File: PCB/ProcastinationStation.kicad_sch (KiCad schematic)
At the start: 19 parts, among them J1 Conn_01x14_Socket, SW1 Up, SW10 X, SW11 L1, SW12 R2, SW13 Right, SW14 Y, SW2 A, SW3 Start, SW4 R1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

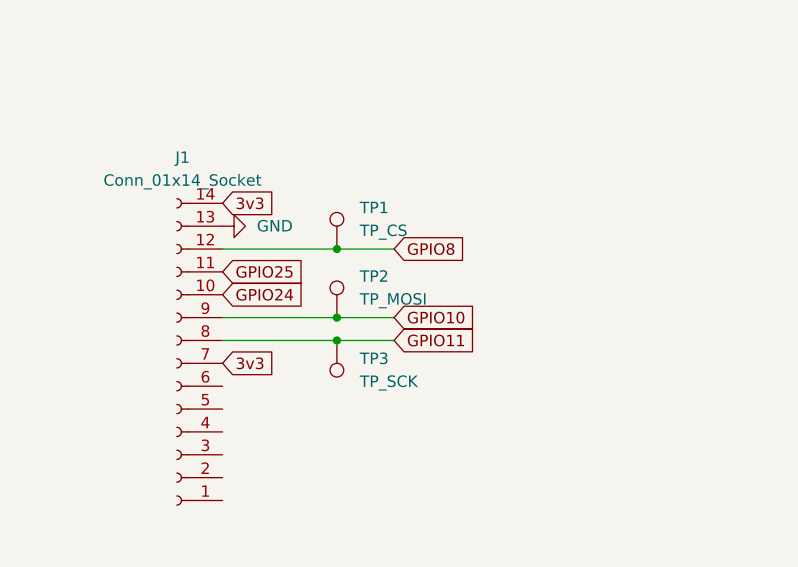
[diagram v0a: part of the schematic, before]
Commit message: Update PCB schematic and layout
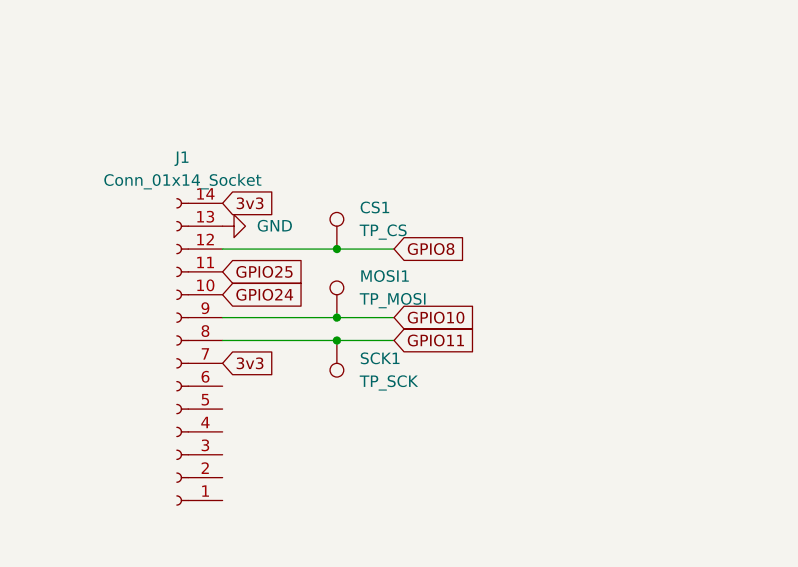
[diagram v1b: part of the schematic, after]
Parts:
- renumbered TP1 to CS1, TP2 to MOSI1, TP3 to SCK1
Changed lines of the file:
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@@
 		(dnp no)
 		(fields_autoplaced yes)
-		(property "Reference" "TP3"
+		(property "Reference" "SCK1"
 			(at 69.85 93.4719 0)
 			(effects
@@
 			(project "ProcastinationStation"
 				(path "/8f9de815-95d5-43c9-a091-d021baccd8d5"
-					(reference "TP3")
+					(reference "SCK1")
 					(unit 1)
 				)
@@
 		(dnp no)
 		(fields_autoplaced yes)
-		(property "Reference" "TP1"
+		(property "Reference" "CS1"
 			(at 69.85 76.7079 0)
 			(effects
@@
 			(project ""
 				(path "/8f9de815-95d5-43c9-a091-d021baccd8d5"
-					(reference "TP1")
+					(reference "CS1")
 					(unit 1)
 				)
@@
 		(dnp no)
 		(fields_autoplaced yes)
-		(property "Reference" "TP2"
+		(property "Reference" "MOSI1"
 			(at 69.85 84.3279 0)
 			(effects
@@
 			(project ""
 				(path "/8f9de815-95d5-43c9-a091-d021baccd8d5"
-					(reference "TP2")
-					(unit 1)
-				)
+					(reference "MOSI1")
+					(unit 1)
+				)
